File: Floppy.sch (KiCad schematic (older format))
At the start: 9 parts, among them IC104 UPD765AC-2, IC105 74LS38, IC106 74LS38, IC107 74HC14

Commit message: finished the centronic 36, some more refinements on placement, new footprint for some connectors
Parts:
- CD104: footprint Connector_PinSocket_2.54mm:PinSocket_2x13_P2.54mm_Vertical -> cpc6128+:Connector_Disk_2x13
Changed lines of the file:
@@
 F 0 "CD104" H 10578 1908 39  0000 L CNN
 F 1 "FDD 26 WAY CONN." H 10578 1833 39  0000 L CNN
-F 2 "Connector_PinSocket_2.54mm:PinSocket_2x13_P2.54mm_Vertical" H 10450 3400 39  0001 C CNN
+F 2 "cpc6128+:Connector_Disk_2x13" H 10450 3400 39  0001 C CNN
 F 3 "" H 10450 3400 39  0001 C CNN
 	1    10450 1900

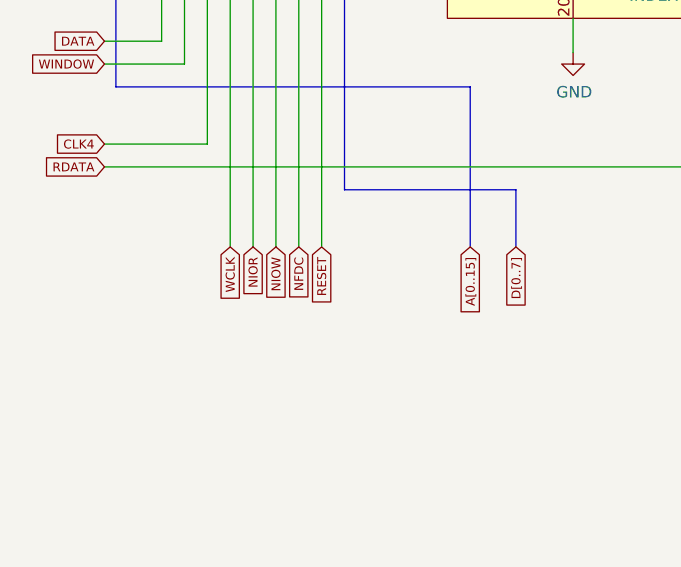
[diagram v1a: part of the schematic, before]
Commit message: 29-03-2021 : first usage of hierarchical labels. focus on CPU/ Cartridge Connector
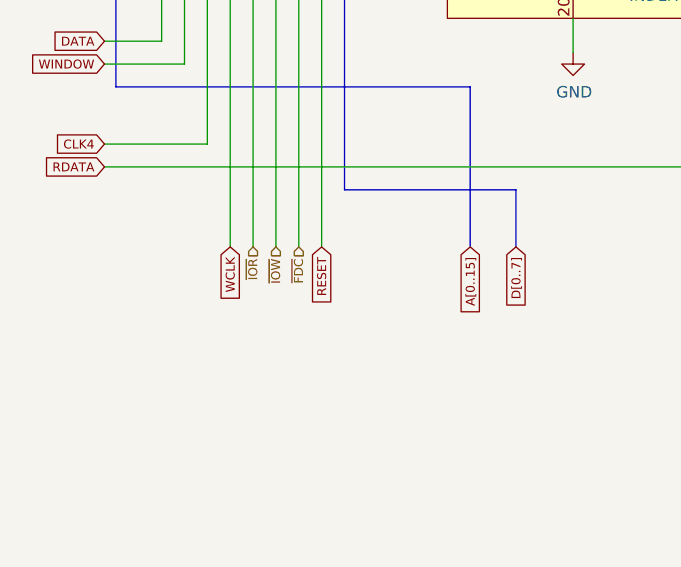
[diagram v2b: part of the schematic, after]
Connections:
- net NFDC renamed ~FDC
- net NIOR renamed ~IOR
- net NIOW renamed ~IOW
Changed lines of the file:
@@
 Text GLabel 1700 5200 3    39   Input ~ 0
 WCLK
-Text GLabel 1800 5200 3    39   Input ~ 0
-NIOR
-Text GLabel 1900 5200 3    39   Input ~ 0
-NIOW
-Text GLabel 2000 5200 3    39   Input ~ 0
-NFDC
 Text GLabel 2100 5200 3    39   Input ~ 0
 RESET
@@
 	9650 4300 9650 5200
 Connection ~ 7550 5250
+Text HLabel 1800 5200 3    39   Input ~ 0
+~IOR
+Text HLabel 1900 5200 3    39   Input ~ 0
+~IOW
+Text HLabel 2000 5200 3    39   Input ~ 0
+~FDC
 Wire Bus Line
 	2200 3400 2200 4950
